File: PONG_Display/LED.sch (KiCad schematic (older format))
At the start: 1 part

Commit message: V3
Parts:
- added C?: 100n, symbol Device:C
- added R?: 180R, symbol Device:R
- added U?: PC817, Package_DIP:DIP-4_W7.62mm, symbol Isolator:PC817
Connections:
- net GND: now also C?.2, U?.2
- net LED_DATA: now also R?.2; no longer J?.2 (Pin_2)
- new net: R?.1, U?.1
- new net +5V: U?.4
- new net LED_DATA_ISO: C?.1, J?.2 (Pin_2), U?.3
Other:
- note added: "Układ izolatora"
- note added: "Złącze wyjścia na wyświetlacz"
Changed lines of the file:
@@
 $Descr A4 11693 8268
 encoding utf-8
-Sheet 4 6
+Sheet 2 6
 Title ""
 Date ""
@@
 $EndComp
 Text GLabel 8550 2800 0    50   Input ~ 0
-LED_DATA
+LED_DATA_ISO
 Wire Wire Line
 	8550 2800 8650 2800
@@
 Schemat wyświetlacza LED
 $Comp
-L power:+12V #PWR?
+L power:+12V #PWR0101
 U 1 1 5E85B748
 P 8500 2550
-F 0 "#PWR?" H 8500 2400 50  0001 C CNN
+F 0 "#PWR0101" H 8500 2400 50  0001 C CNN
 F 1 "+12V" H 8515 2723 50  0000 C CNN
 F 2 "" H 8500 2550 50  0001 C CNN
@@
 $EndComp
 $Comp
-L power:GND #PWR?
+L power:GND #PWR0102
 U 1 1 5E85BD1D
 P 8500 3050
-F 0 "#PWR?" H 8500 2800 50  0001 C CNN
+F 0 "#PWR0102" H 8500 2800 50  0001 C CNN
 F 1 "GND" H 8505 2877 50  0000 C CNN
 F 2 "" H 8500 3050 50  0001 C CNN
@@
 Wire Wire Line
 	8500 2900 8650 2900
+Text Notes 8250 2000 0    50   ~ 0
+Złącze wyjścia na wyświetlacz
+Text GLabel 1900 2550 0    50   Input ~ 0
+LED_DATA
+$Comp
+L Isolator:PC817 U?
+U 1 1 5E9027A7
+P 2950 2650
+F 0 "U?" H 2950 2975 50  0000 C CNN
+F 1 "PC817" H 2950 2884 50  0000 C CNN
+F 2 "Package_DIP:DIP-4_W7.62mm" H 2750 2450 50  0001 L CIN
+F 3 "http://www.soselectronic.cz/a_info/resource/d/pc817.pdf" H 2950 2650 50  0001 L CNN
+	1    2950 2650
+	1    0    0    -1
+$EndComp
+$Comp
+L Device:R R?
+U 1 1 5E90451D
+P 2200 2550
+F 0 "R?" V 1993 2550 50  0000 C CNN
+F 1 "180R" V 2084 2550 50  0000 C CNN
+F 2 "" V 2130 2550 50  0001 C CNN
+F 3 "~" H 2200 2550 50  0001 C CNN
+	1    2200 2550
+	0    1    1    0
+$EndComp
+$Comp
+L power:GND #PWR0103
+U 1 1 5E9048A0
+P 2450 3200
+F 0 "#PWR0103" H 2450 2950 50  0001 C CNN
+F 1 "GND" H 2455 3027 50  0000 C CNN
+F 2 "" H 2450 3200 50  0001 C CNN
+F 3 "" H 2450 3200 50  0001 C CNN
+	1    2450 3200
+	1    0    0    -1
+$EndComp
+$Comp
+L power:+5V #PWR0104
+U 1 1 5E904C1B
+P 3500 2300
+F 0 "#PWR0104" H 3500 2150 50  0001 C CNN
+F 1 "+5V" H 3515 2473 50  0000 C CNN
+F 2 "" H 3500 2300 50  0001 C CNN
+F 3 "" H 3500 2300 50  0001 C CNN
+	1    3500 2300
+	1    0    0    -1
+$EndComp
+Text GLabel 3600 2750 2    50   Output ~ 0
+LED_DATA_ISO
+Wire Wire Line
+	1900 2550 2050 2550
+Wire Wire Line
+	2350 2550 2650 2550
+Wire Wire Line
+	2450 3200 2450 2750
+Wire Wire Line
+	2450 2750 2650 2750
+Wire Wire Line
+	3250 2550 3500 2550
+Wire Wire Line
+	3500 2550 3500 2300
+Wire Wire Line
+	3250 2750 3400 2750
+Wire Notes Line
+	1150 1050 4800 1050
+Wire Notes Line
+	4800 1050 4800 3850
+Wire Notes Line
+	4800 3850 1150 3850
+Wire Notes Line
+	1150 3850 1150 1050
+Text Notes 1950 1350 0    50   ~ 0
+Układ izolatora
+$Comp
+L Device:C C?
+U 1 1 5E90693A
+P 3400 2950
+F 0 "C?" H 3515 2996 50  0000 L CNN
+F 1 "100n" H 3515 2905 50  0000 L CNN
+F 2 "" H 3438 2800 50  0001 C CNN
+F 3 "~" H 3400 2950 50  0001 C CNN
+	1    3400 2950
+	1    0    0    -1
+$EndComp
+$Comp
+L power:GND #PWR0105
+U 1 1 5E906F7A
+P 3400 3200
+F 0 "#PWR0105" H 3400 2950 50  0001 C CNN
+F 1 "GND" H 3405 3027 50  0000 C CNN
+F 2 "" H 3400 3200 50  0001 C CNN
+F 3 "" H 3400 3200 50  0001 C CNN
+	1    3400 3200
+	1    0    0    -1
+$EndComp
+Wire Wire Line
+	3400 2750 3400 2800
+Connection ~ 3400 2750
+Wire Wire Line
+	3400 2750 3600 2750
+Wire Wire Line
+	3400 3100 3400 3200
 $EndSCHEMATC

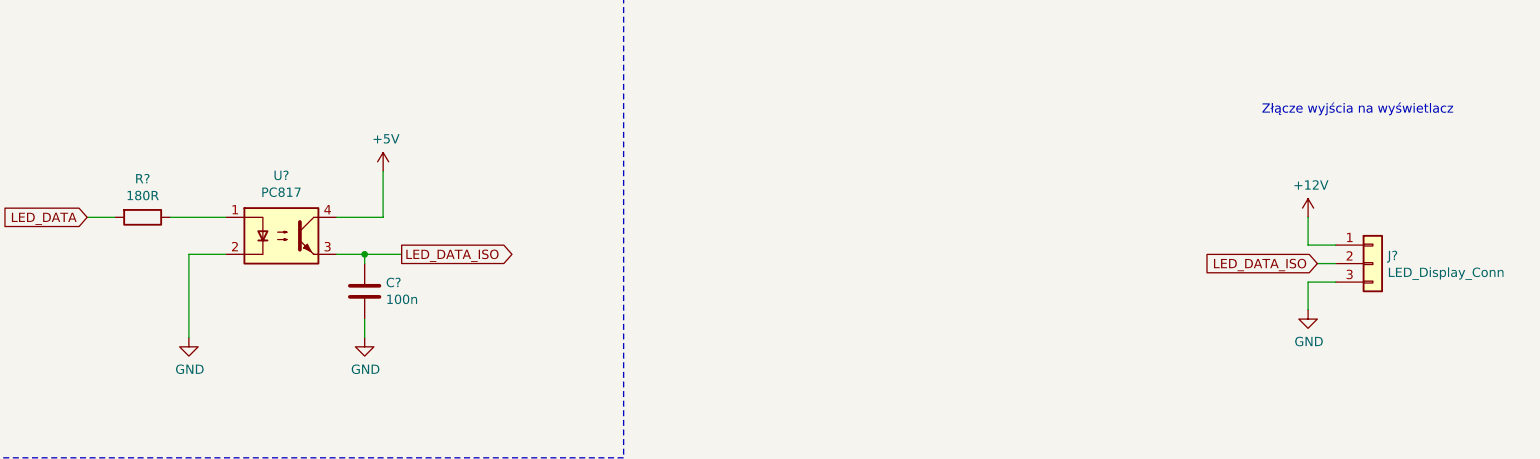
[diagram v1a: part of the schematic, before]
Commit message: Dodane footprinty
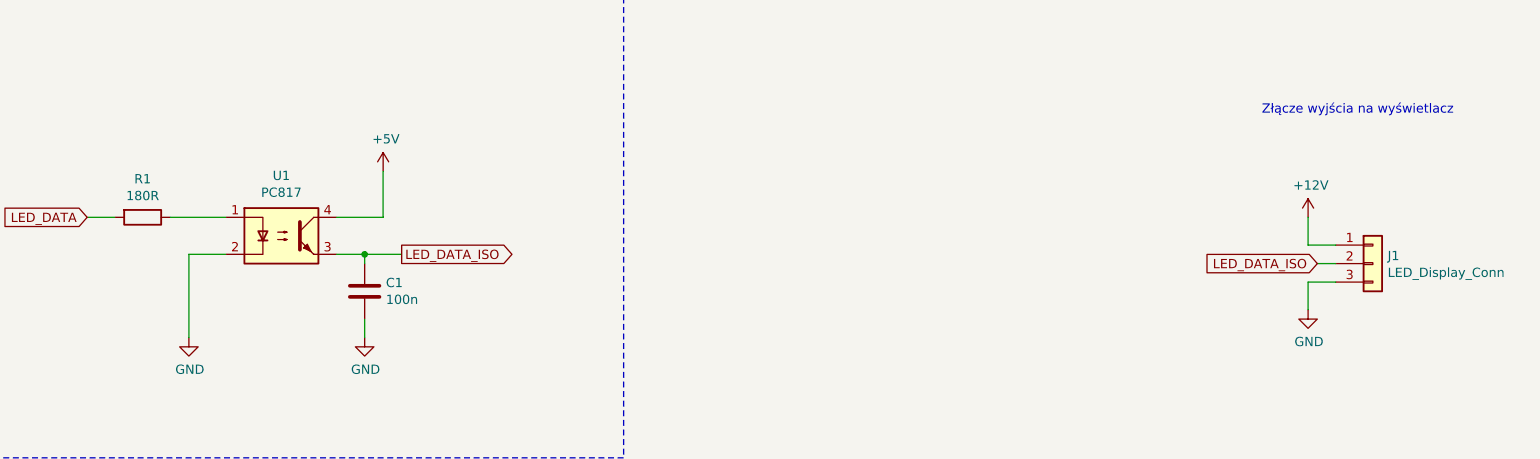
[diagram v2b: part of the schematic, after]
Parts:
- C1: renamed from C?; footprint (none) -> Capacitor_SMD:C_1206_3216Metric_Pad1.42x1.75mm_HandSolder
- R1: renamed from R?; footprint (none) -> Resistor_SMD:R_1206_3216Metric_Pad1.42x1.75mm_HandSolder
- gave numbers to parts that had none: 2
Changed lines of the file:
@@
 P 8850 2800
 AR Path="/5E80CCDD/5E83917B" Ref="J?"  Part="1"
-AR Path="/5E80C133/5E83917B" Ref="J?"  Part="1"
-F 0 "J?" H 8930 2842 50  0000 L CNN
+AR Path="/5E80C133/5E83917B" Ref="J1"  Part="1"
+F 0 "J1" H 8930 2842 50  0000 L CNN
 F 1 "LED_Display_Conn" H 8930 2751 50  0000 L CNN
 F 2 "" H 8850 2800 50  0001 C CNN
@@
 LED_DATA
 $Comp
-L Isolator:PC817 U?
+L Isolator:PC817 U1
 U 1 1 5E9027A7
 P 2950 2650
-F 0 "U?" H 2950 2975 50  0000 C CNN
+F 0 "U1" H 2950 2975 50  0000 C CNN
 F 1 "PC817" H 2950 2884 50  0000 C CNN
 F 2 "Package_DIP:DIP-4_W7.62mm" H 2750 2450 50  0001 L CIN
@@
 $EndComp
 $Comp
-L Device:R R?
+L Device:R R1
 U 1 1 5E90451D
 P 2200 2550
-F 0 "R?" V 1993 2550 50  0000 C CNN
+F 0 "R1" V 1993 2550 50  0000 C CNN
 F 1 "180R" V 2084 2550 50  0000 C CNN
-F 2 "" V 2130 2550 50  0001 C CNN
+F 2 "Resistor_SMD:R_1206_3216Metric_Pad1.42x1.75mm_HandSolder" V 2130 2550 50  0001 C CNN
 F 3 "~" H 2200 2550 50  0001 C CNN
 	1    2200 2550
@@
 Układ izolatora
 $Comp
-L Device:C C?
+L Device:C C1
 U 1 1 5E90693A
 P 3400 2950
-F 0 "C?" H 3515 2996 50  0000 L CNN
+F 0 "C1" H 3515 2996 50  0000 L CNN
 F 1 "100n" H 3515 2905 50  0000 L CNN
-F 2 "" H 3438 2800 50  0001 C CNN
+F 2 "Capacitor_SMD:C_1206_3216Metric_Pad1.42x1.75mm_HandSolder" H 3438 2800 50  0001 C CNN
 F 3 "~" H 3400 2950 50  0001 C CNN
 	1    3400 2950

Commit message: Drobne zmiany
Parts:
- J1: footprint (none) -> TerminalBlock:TerminalBlock_bornier-3_P5.08mm
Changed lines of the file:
@@
 F 0 "J1" H 8930 2842 50  0000 L CNN
 F 1 "LED_Display_Conn" H 8930 2751 50  0000 L CNN
-F 2 "" H 8850 2800 50  0001 C CNN
+F 2 "TerminalBlock:TerminalBlock_bornier-3_P5.08mm" H 8850 2800 50  0001 C CNN
 F 3 "~" H 8850 2800 50  0001 C CNN
 	1    8850 2800

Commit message: Teraz jest sexy
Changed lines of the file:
@@
 EESchema Schematic File Version 4
+LIBS:PONG_Display-cache
 EELAYER 30 0
 EELAYER END
@@
 	1    0    0    -1
 $EndComp
-Text GLabel 8550 2800 0    50   Input ~ 0
-LED_DATA_ISO
-Wire Wire Line
-	8550 2800 8650 2800
 Text Notes 7750 7500 0    50   ~ 0
 Schemat wyświetlacza LED
@@
 Text Notes 8250 2000 0    50   ~ 0
 Złącze wyjścia na wyświetlacz
-Text GLabel 1900 2550 0    50   Input ~ 0
-LED_DATA
 $Comp
 L Isolator:PC817 U1
@@
 	1    0    0    -1
 $EndComp
-Text GLabel 3600 2750 2    50   Output ~ 0
-LED_DATA_ISO
-Wire Wire Line
-	1900 2550 2050 2550
 Wire Wire Line
 	2350 2550 2650 2550
@@
 Wire Wire Line
 	3400 3100 3400 3200
+Text HLabel 1900 2550 0    50   Input ~ 0
+LED_DATA
+Text Label 3600 2750 0    50   ~ 0
+LED_DATA_ISO
+Text Label 7950 2800 0    50   ~ 0
+LED_DATA_ISO
+Wire Wire Line
+	7950 2800 8650 2800
+Wire Wire Line
+	1900 2550 2050 2550
 $EndSCHEMATC

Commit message: 2
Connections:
- net +5V is gone; now on net +12V: U1.4
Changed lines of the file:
@@
 EESchema Schematic File Version 4
-LIBS:PONG_Display-cache
 EELAYER 30 0
 EELAYER END
@@
 	1    0    0    -1
 $EndComp
-$Comp
-L power:+5V #PWR0104
-U 1 1 5E904C1B
-P 3500 2300
-F 0 "#PWR0104" H 3500 2150 50  0001 C CNN
-F 1 "+5V" H 3515 2473 50  0000 C CNN
-F 2 "" H 3500 2300 50  0001 C CNN
-F 3 "" H 3500 2300 50  0001 C CNN
-	1    3500 2300
-	1    0    0    -1
-$EndComp
 Wire Wire Line
 	2350 2550 2650 2550
@@
 Wire Wire Line
 	1900 2550 2050 2550
+$Comp
+L power:+12V #PWR0104
+U 1 1 5E9C9DE1
+P 3500 2300
+F 0 "#PWR0104" H 3500 2150 50  0001 C CNN
+F 1 "+12V" H 3515 2473 50  0000 C CNN
+F 2 "" H 3500 2300 50  0001 C CNN
+F 3 "" H 3500 2300 50  0001 C CNN
+	1    3500 2300
+	1    0    0    -1
+$EndComp
 $EndSCHEMATC
